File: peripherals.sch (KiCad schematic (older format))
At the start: 41 parts, among them J10 Conn_Speaker, J9 Micro_SD_Card_Det, Q6 BSS138, Q7 BSS138, Q8 BSS138, SW3 SW_USR, U4 IS25LP128F, U5 DMC2450, U6 DMC2450

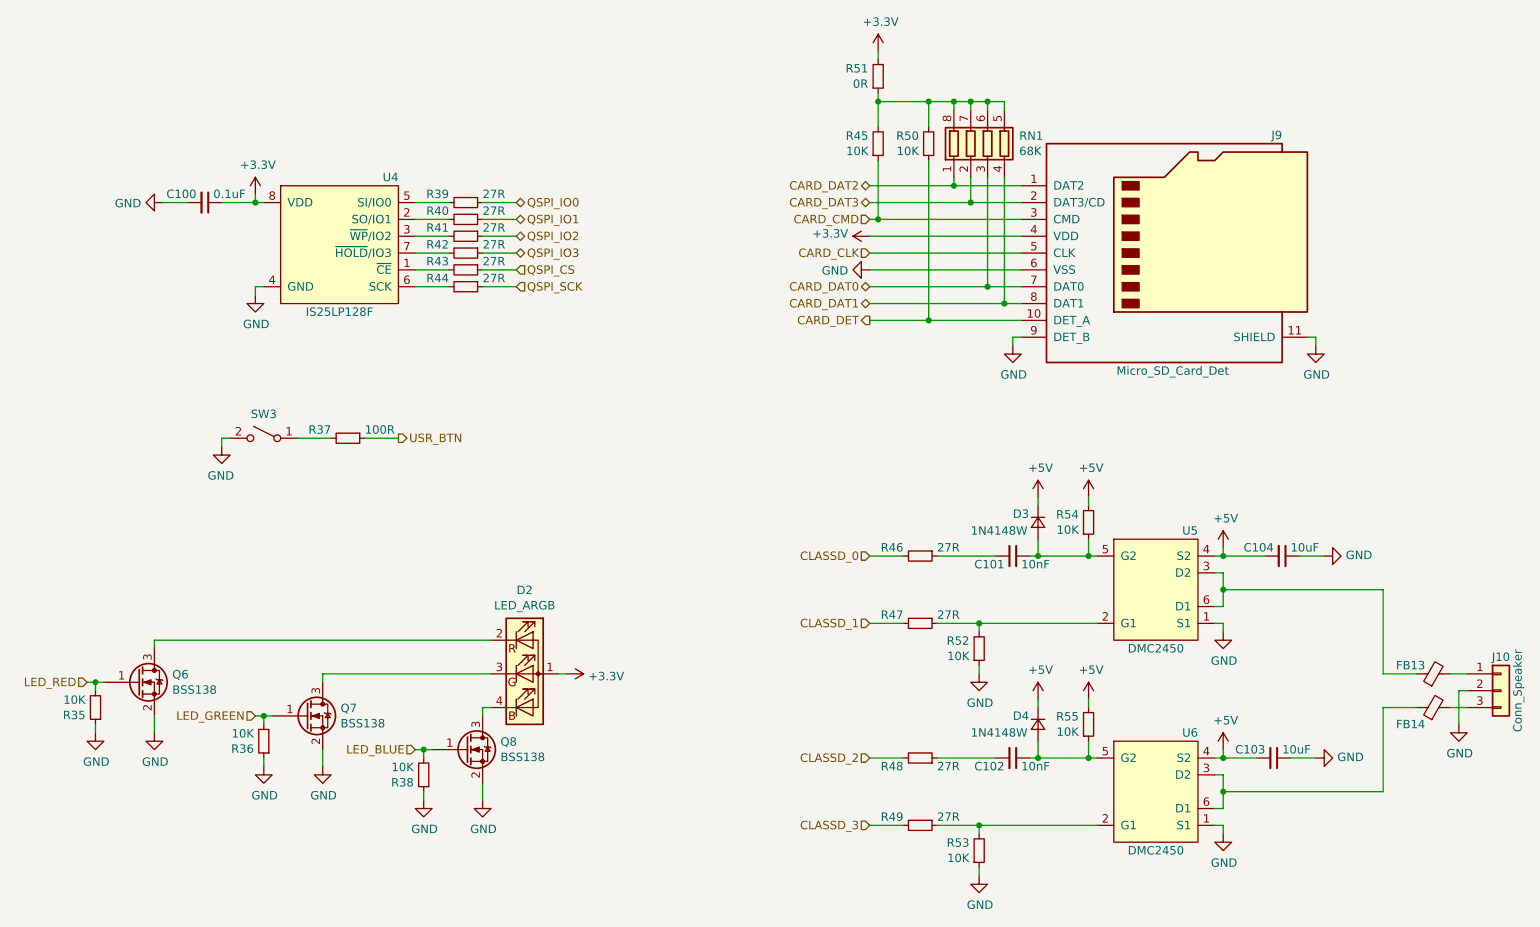
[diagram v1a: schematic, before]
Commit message: More routing, 165 unconnected left
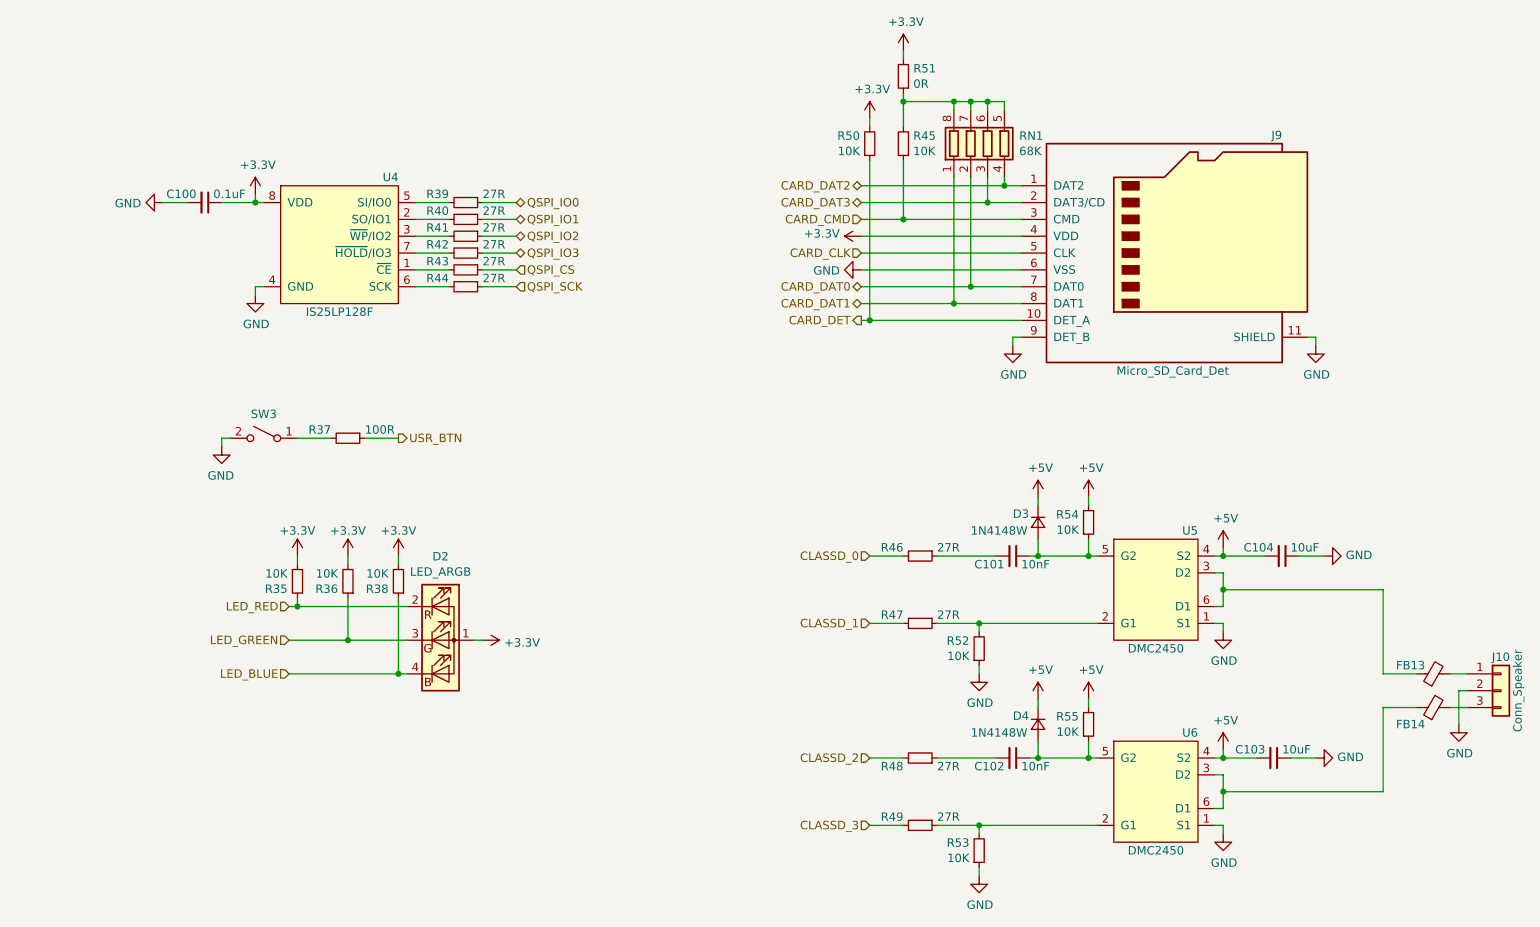
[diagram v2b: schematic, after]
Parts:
- removed Q6, Q7, Q8: BSS138, Package_TO_SOT_SMD:SOT-23, symbol Transistor_FET:BSS138
- FB13, FB14: value 10R 1A -> BLM18PG300SN1D
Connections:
- net +3V3: now also R35.2, R36.2, R38.2, R50.2
- net CARD_DAT0: now also RN1.2 (R2.1); no longer RN1.3 (R3.1)
- net CARD_DAT1: now also RN1.1 (R1.1); no longer RN1.4 (R4.1)
- net CARD_DAT2: now also RN1.4 (R4.1); no longer RN1.1 (R1.1)
- net CARD_DAT3: now also RN1.3 (R3.1); no longer RN1.2 (R2.1)
- net GND: no longer R35.1, R36.1, R38.1
- net LED_BLUE: now also D2.4 (BK), R38.1; no longer R38.2
- net LED_GREEN: now also D2.3 (GK), R36.1; no longer R36.2
- net LED_RED: now also D2.2 (RK), R35.1; no longer R35.2
- net at R45.2, R51.1, RN1.5 (R4.2)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: no longer R50.2
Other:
- moved on the sheet: D2, R35, R36, R38, R45, R50, R51
